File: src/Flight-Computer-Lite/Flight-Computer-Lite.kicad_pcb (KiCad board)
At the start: 4 copper layers, 66.8 x 25.4 mm, 61 parts, among them J1 Jumper_NO, P1 CONN_1984659_PXC, P2 USB, P3 0530470610, P4 1546551-2, Q1 QS5U17TR, Q2 2N7002W-7-F, Q3 2N7002W-7-F, Q4 QS5U17TR, Q5 2N7002W-7-F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

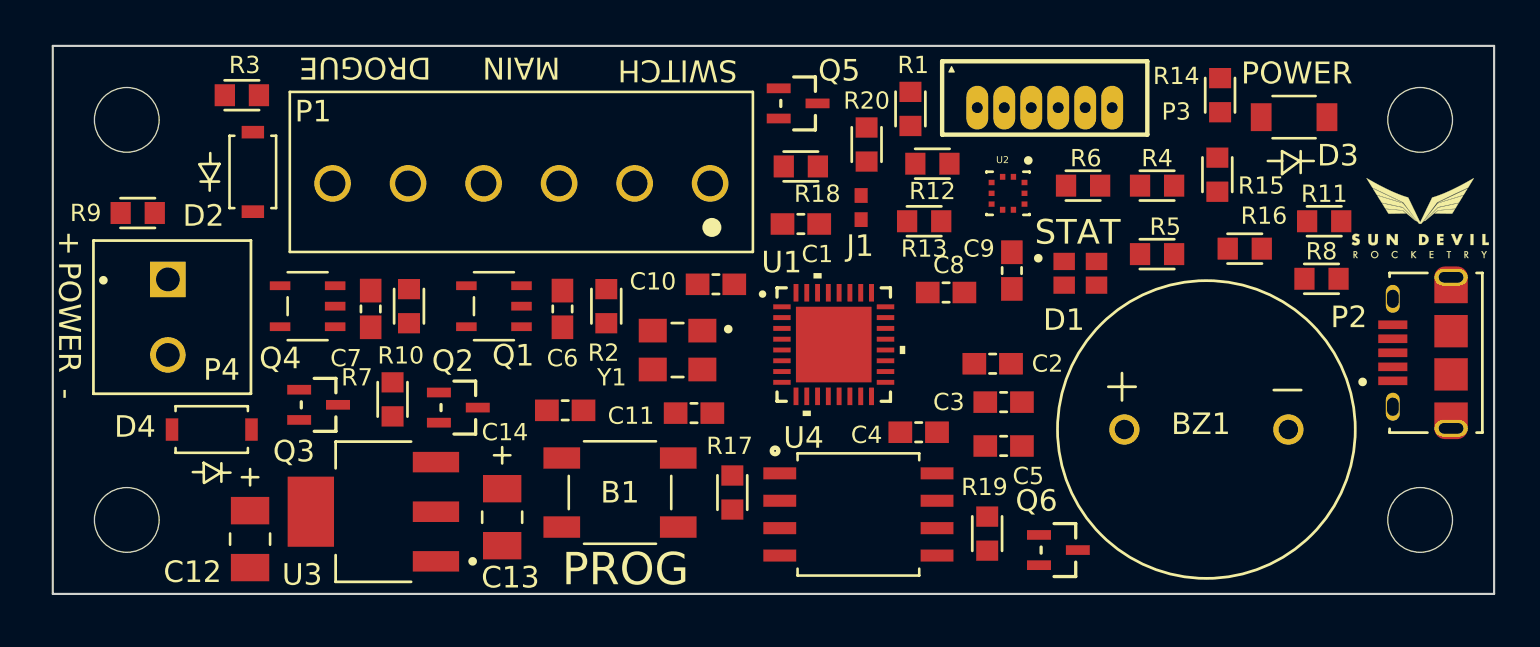
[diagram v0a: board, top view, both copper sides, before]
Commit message: began PCB routing
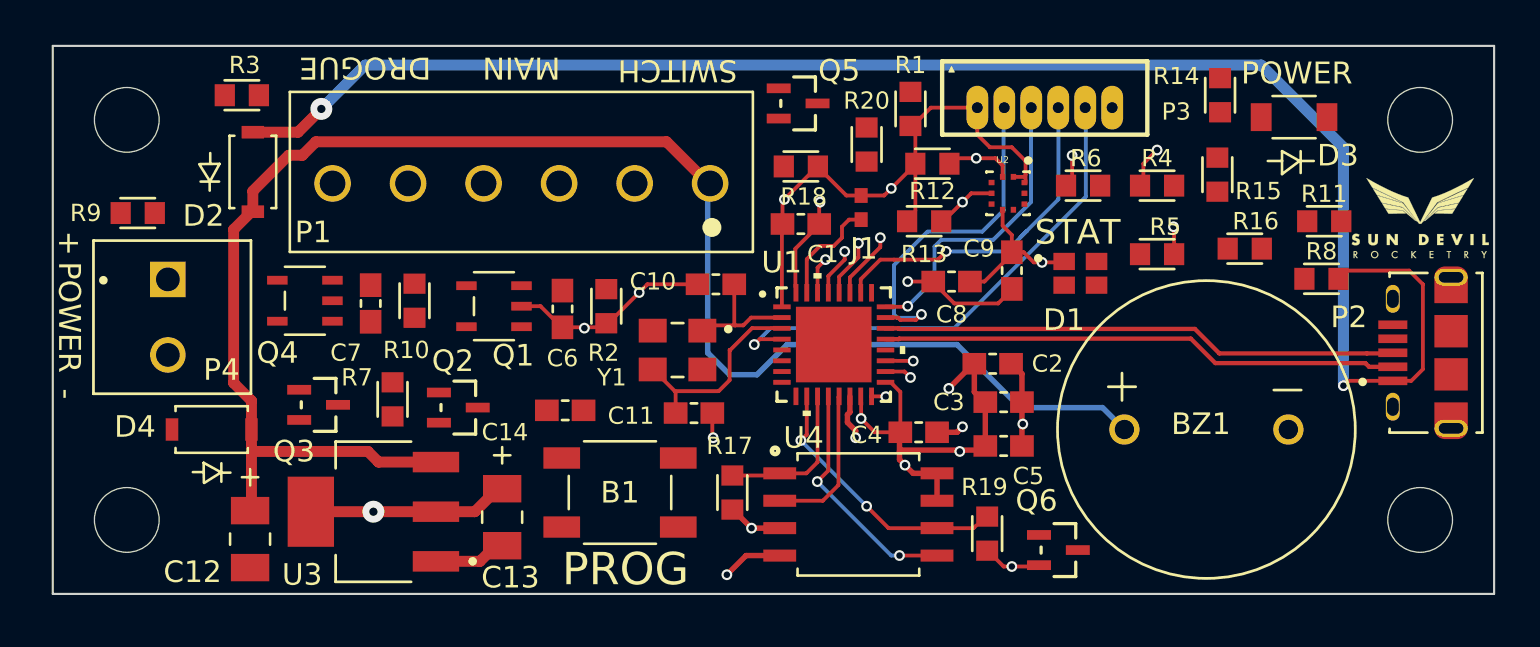
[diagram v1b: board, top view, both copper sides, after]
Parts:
- moved C8 0.57 mm to (192.5, 96.0), turned to 180 degrees
- moved R10 0.36 mm to (167.6, 96.9)
- moved Q4 0.28 mm to (162.6, 96.9)
- moved C7 0.25 mm to (165.6, 97.0)
- turned C1 to 0 degrees
- turned R1 to -90 degrees
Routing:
- net 5V: track 0.00 -> 76.4 mm, vias 0 -> 2
- net VIN: track 0.00 -> 76.1 mm
- net 3.3V: track 0.07 -> 61.0 mm, vias 0 -> 9
- net Earth: track 0.00 -> 34.7 mm, vias 0 -> 11
- net STATUS_B: track 0.00 -> 27.1 mm, vias 0 -> 2
- net STATUS_G: track 0.00 -> 24.7 mm, vias 0 -> 2
- net USB_D-: track 0.00 -> 24.1 mm
- net NRST: track 0.00 -> 23.8 mm, vias 0 -> 1
- net USB_D+: track 0.00 -> 23.6 mm
- net SWDIO: track 0.00 -> 16.3 mm, vias 0 -> 1
- net STATUS_R: track 0.00 -> 16.1 mm, vias 0 -> 2
- net SWO: track 0.00 -> 16.0 mm, vias 0 -> 1
- net BP_SCL: track 0.00 -> 14.9 mm, vias 0 -> 2
- net SWCLK: track 0.00 -> 14.1 mm, vias 0 -> 1
- net BP_SDA: track 0.00 -> 13.2 mm, vias 0 -> 2
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
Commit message: finished initial routing
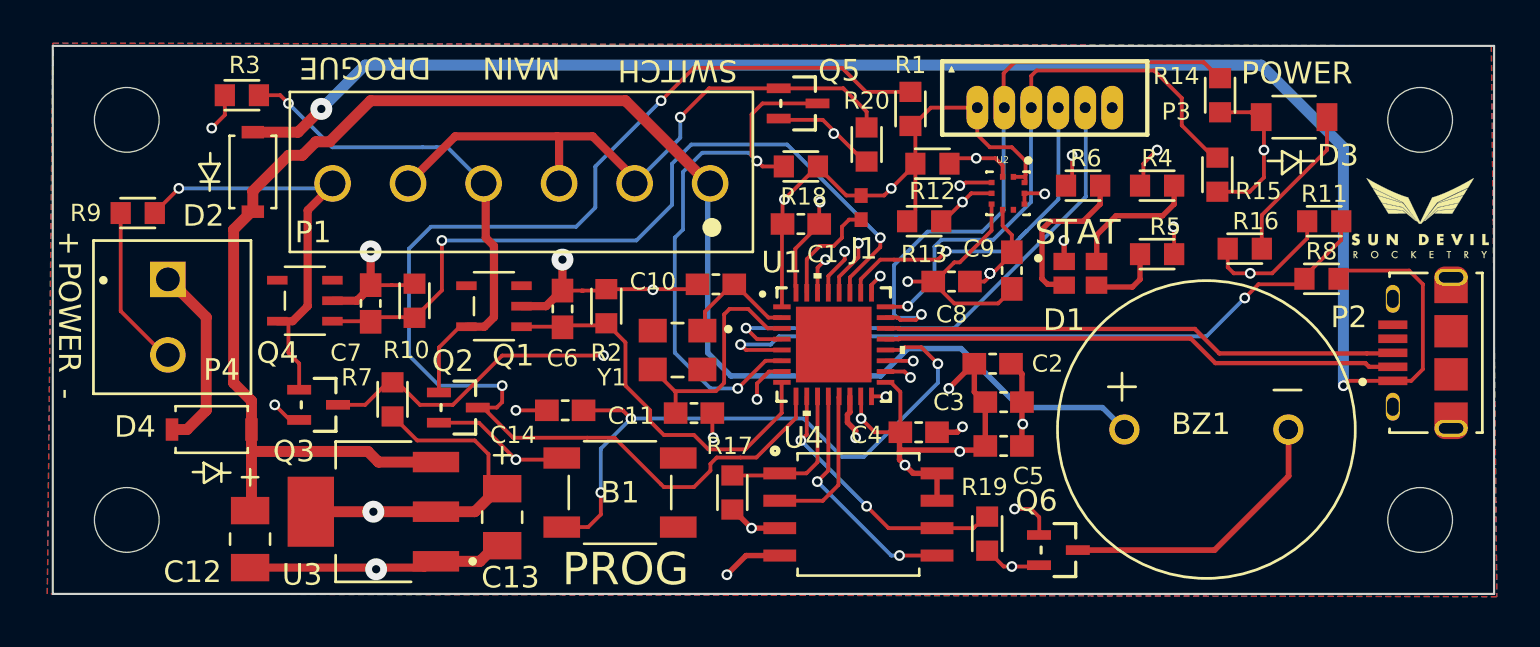
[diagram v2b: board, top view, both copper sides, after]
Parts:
- turned C14 to 180 degrees
- turned C6 to 90 degrees
- turned R2 to -90 degrees
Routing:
- net ~{MAIN_CONT}: track 0.00 -> 58.9 mm, vias 0 -> 2
- net Earth: track 34.7 -> 86.2 mm, vias 11 -> 21
- net DROGUE: track 3.14 -> 36.1 mm, vias 1 -> 2
- net USB_DETECT: track 0.00 -> 32.3 mm, vias 0 -> 2
- net ~{DROGUE_CONT}: track 0.00 -> 30.4 mm, vias 0 -> 2
- net PROG: track 0.00 -> 29.5 mm, vias 0 -> 3
- net VIN_SW: track 0.00 -> 28.8 mm, vias 0 -> 1
- net ~{SWITCH}: track 0.00 -> 25.3 mm, vias 0 -> 2
- net Net-(P1-Pad4): track 0.00 -> 23.4 mm, vias 0 -> 1
- net Net-(P1-Pad6): track 0.00 -> 19.5 mm, vias 0 -> 1
- net BEEP: track 0.00 -> 18.2 mm, vias 0 -> 2
- net MAIN: track 0.00 -> 18.0 mm
- net Net-(BZ1-Pad2): track 0.00 -> 13.3 mm
- net SWCLK: track 14.1 -> 26.9 mm
- net SWDIO: track 16.3 -> 28.4 mm
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- added copper zone on In2.Cu, net 3.3V
- added copper zone on B.Cu, net Earth
- added copper zone on F.Cu, net Earth
- added copper zone on In1.Cu, net Earth
